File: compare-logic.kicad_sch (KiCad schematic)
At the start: 18 parts, among them U21001 4069, U21002 4019

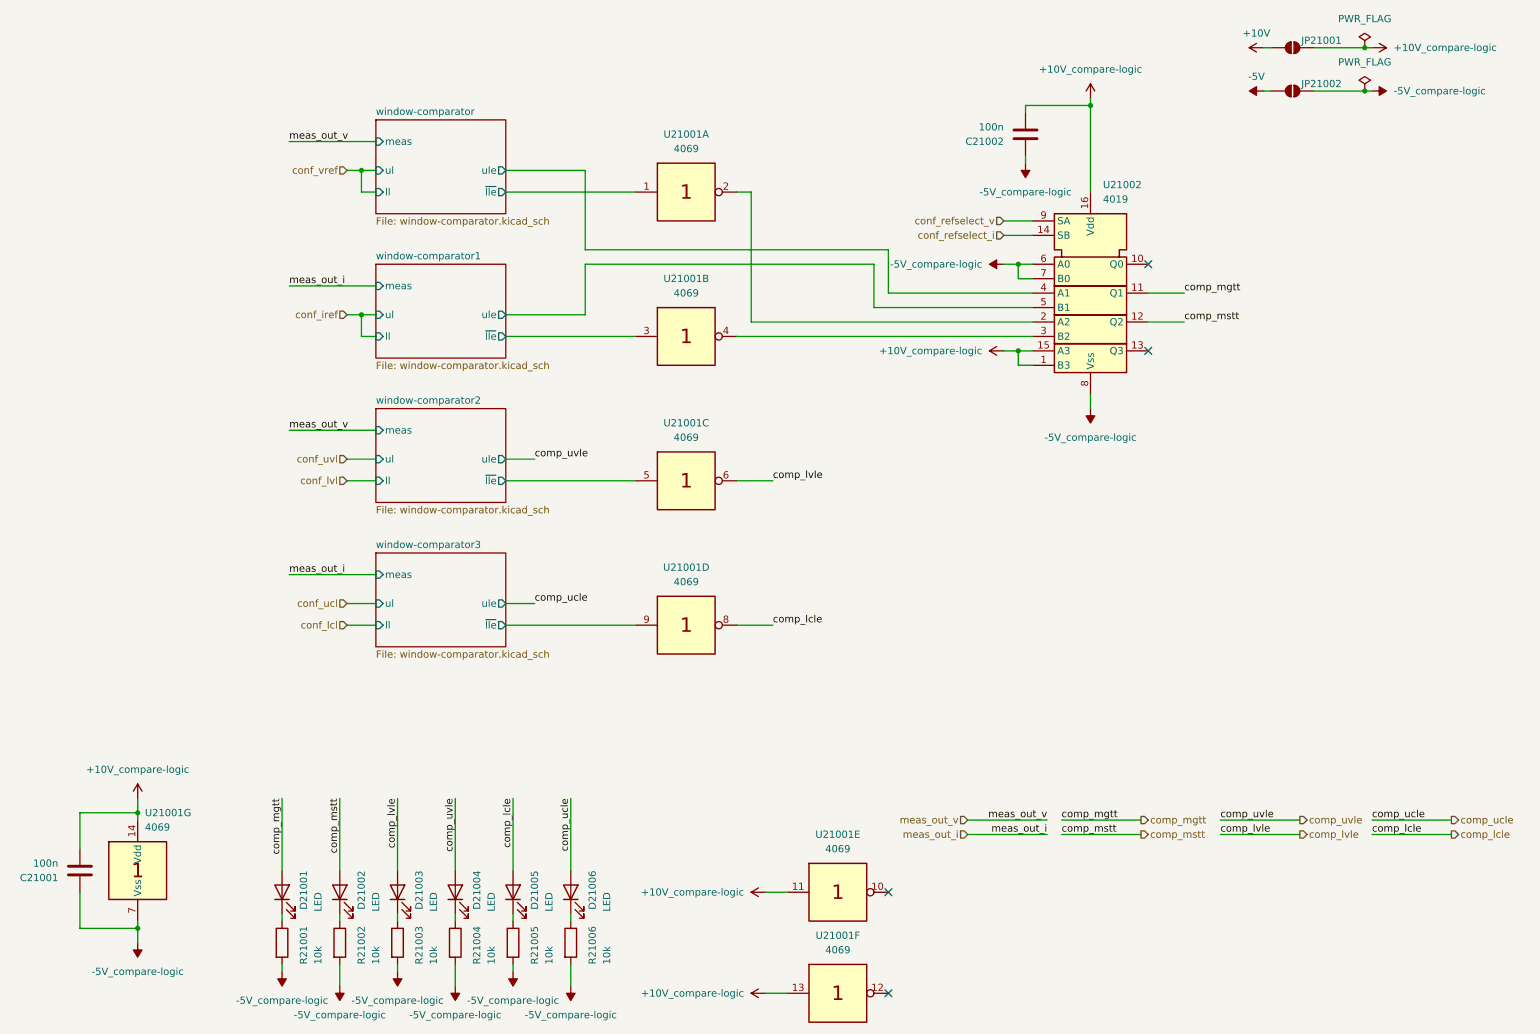
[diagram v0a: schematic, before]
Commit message: add pss 3dmodels and testpoints
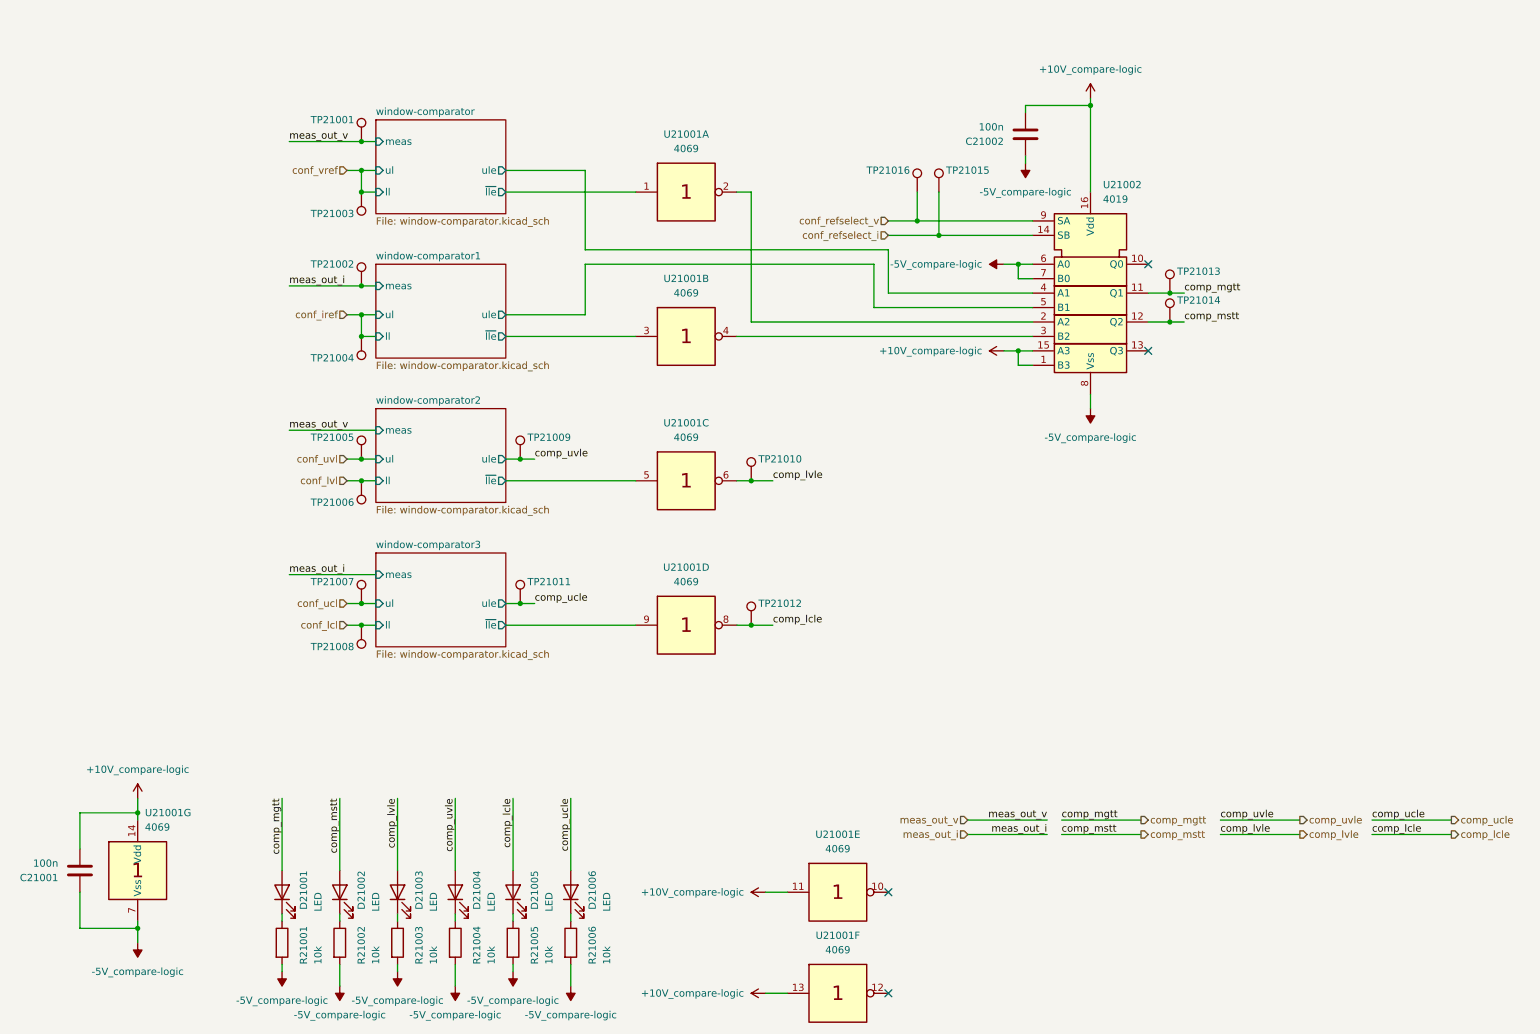
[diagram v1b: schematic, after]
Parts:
- removed JP21001, JP21002: SolderJumper_2_Open, symbol Jumper:SolderJumper_2_Open
- added TP21001, TP21002, TP21003, TP21004, TP21005, TP21006, TP21007, TP21008, TP21009, TP21010, TP21011, TP21012, TP21013, TP21014, TP21015, TP21016: ~, pss:TP_0805_2012Metric, symbol Connector:TestPoint
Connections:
- net comp_lcle: now also TP21012.1
- net comp_lvle: now also TP21010.1
- net comp_mgtt: now also TP21013.1
- net comp_mstt: now also TP21014.1
- net comp_ucle: now also TP21011.1
- net comp_uvle: now also TP21009.1
- net conf_iref: now also TP21004.1
- net conf_lcl: now also TP21008.1
- net conf_lvl: now also TP21006.1
- net conf_refselect_i: now also TP21015.1
- net conf_refselect_v: now also TP21016.1
- net conf_ucl: now also TP21007.1
- net conf_uvl: now also TP21005.1
- net conf_vref: now also TP21003.1
- net meas_out_i: now also TP21002.1
- net meas_out_v: now also TP21001.1

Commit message: edit pss symbol library: export all schematic symbols to library 'pss' and update symbol link
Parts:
- D21001, D21002, D21003, D21004, D21005, D21006: symbol Device:LED -> pss:LED
- TP21001, TP21002, TP21003, TP21004, TP21005, TP21006, TP21007, TP21008, TP21009, TP21010, TP21011, TP21012, TP21013, TP21014, TP21015, TP21016: symbol Connector:TestPoint -> pss:TestPoint
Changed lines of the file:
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@@
 	)
 	(symbol
-		(lib_id "Connector:TestPoint")
+		(lib_id "pss:TestPoint")
 		(at 222.25 67.31 0)
 		(unit 1)
@@
 	)
 	(symbol
-		(lib_id "Connector:TestPoint")
+		(lib_id "pss:TestPoint")
 		(at 181.61 49.53 0)
 		(unit 1)
@@
 	)
 	(symbol
-		(lib_id "Connector:TestPoint")
+		(lib_id "pss:TestPoint")
 		(at 80.01 125.73 180)
 		(unit 1)
@@
 	)
 	(symbol
-		(lib_id "Device:LED")
+		(lib_id "pss:LED")
 		(at 116.84 172.72 90)
 		(unit 1)
@@
 	)
 	(symbol
-		(lib_id "Connector:TestPoint")
+		(lib_id "pss:TestPoint")
 		(at 80.01 49.53 180)
 		(unit 1)
@@
 	)
 	(symbol
-		(lib_id "Connector:TestPoint")
+		(lib_id "pss:TestPoint")
 		(at 177.8 49.53 0)
 		(mirror y)
@@
 	)
 	(symbol
-		(lib_id "Connector:TestPoint")
+		(lib_id "pss:TestPoint")
 		(at 107.95 121.92 0)
 		(unit 1)
@@
 	)
 	(symbol
-		(lib_id "Connector:TestPoint")
+		(lib_id "pss:TestPoint")
 		(at 80.01 66.04 0)
 		(mirror y)
@@
 	)
 	(symbol
-		(lib_id "Connector:TestPoint")
+		(lib_id "pss:TestPoint")
 		(at 80.01 100.33 180)
 		(unit 1)
@@
 	)
 	(symbol
-		(lib_id "Device:LED")
+		(lib_id "pss:LED")
 		(at 96.52 172.72 90)
 		(unit 1)
@@
 	)
 	(symbol
-		(lib_id "Connector:TestPoint")
+		(lib_id "pss:TestPoint")
 		(at 107.95 96.52 0)
 		(unit 1)
@@
 	)
 	(symbol
-		(lib_id "Connector:TestPoint")
+		(lib_id "pss:TestPoint")
 		(at 80.01 121.92 0)
 		(mirror y)
@@
 	)
 	(symbol
-		(lib_id "Connector:TestPoint")
+		(lib_id "pss:TestPoint")
 		(at 80.01 74.93 180)
 		(unit 1)
@@
 	)
 	(symbol
-		(lib_id "Connector:TestPoint")
+		(lib_id "pss:TestPoint")
 		(at 80.01 96.52 0)
 		(mirror y)
@@
 	)
 	(symbol
-		(lib_id "Connector:TestPoint")
+		(lib_id "pss:TestPoint")
 		(at 222.25 72.39 0)
 		(unit 1)
@@
 	)
 	(symbol
-		(lib_id "Device:LED")
+		(lib_id "pss:LED")
 		(at 76.2 172.72 90)
 		(unit 1)
@@
 	)
 	(symbol
-		(lib_id "Connector:TestPoint")
+		(lib_id "pss:TestPoint")
 		(at 148.59 125.73 0)
 		(unit 1)
@@
 	)
 	(symbol
-		(lib_id "Device:LED")
+		(lib_id "pss:LED")
 		(at 106.68 172.72 90)
 		(unit 1)
@@
 	)
 	(symbol
-		(lib_id "Connector:TestPoint")
+		(lib_id "pss:TestPoint")
 		(at 80.01 40.64 0)
 		(mirror y)
@@
 	)
 	(symbol
-		(lib_id "Device:LED")
+		(lib_id "pss:LED")
 		(at 66.04 172.72 90)
 		(unit 1)
@@
 	)
 	(symbol
-		(lib_id "Connector:TestPoint")
+		(lib_id "pss:TestPoint")
 		(at 148.59 100.33 0)
 		(unit 1)
@@
 	)
 	(symbol
-		(lib_id "Device:LED")
+		(lib_id "pss:LED")
 		(at 86.36 172.72 90)
 		(unit 1)

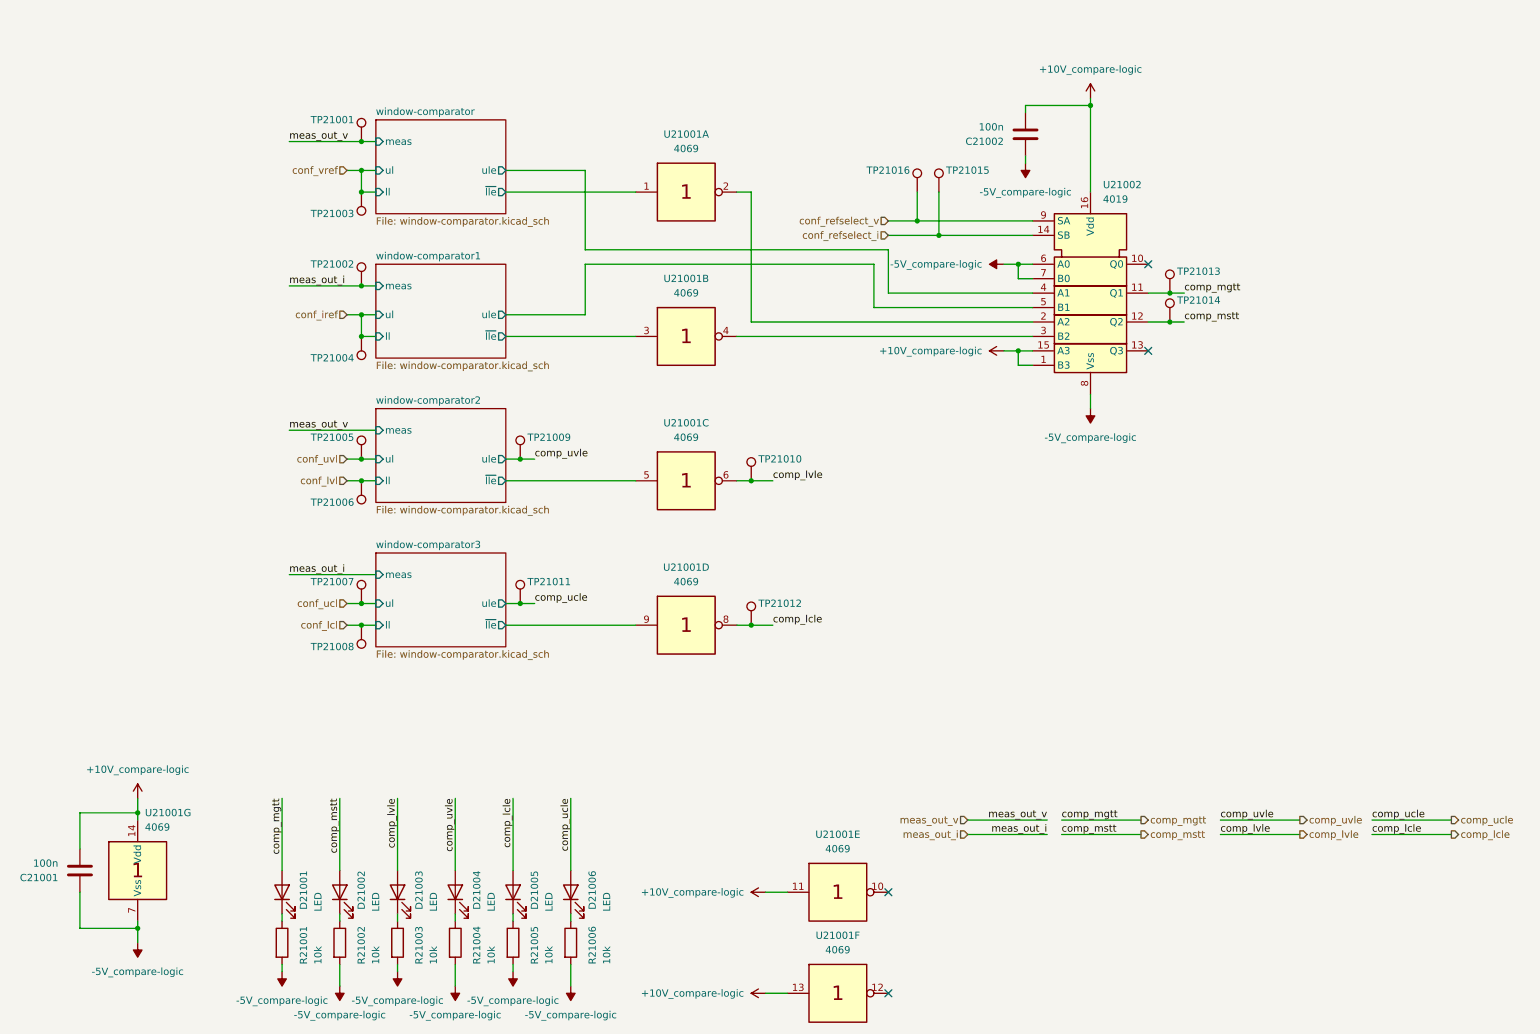
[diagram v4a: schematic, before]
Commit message: edit pss footprint library: export all footprints to library 'pss' and update footprint links
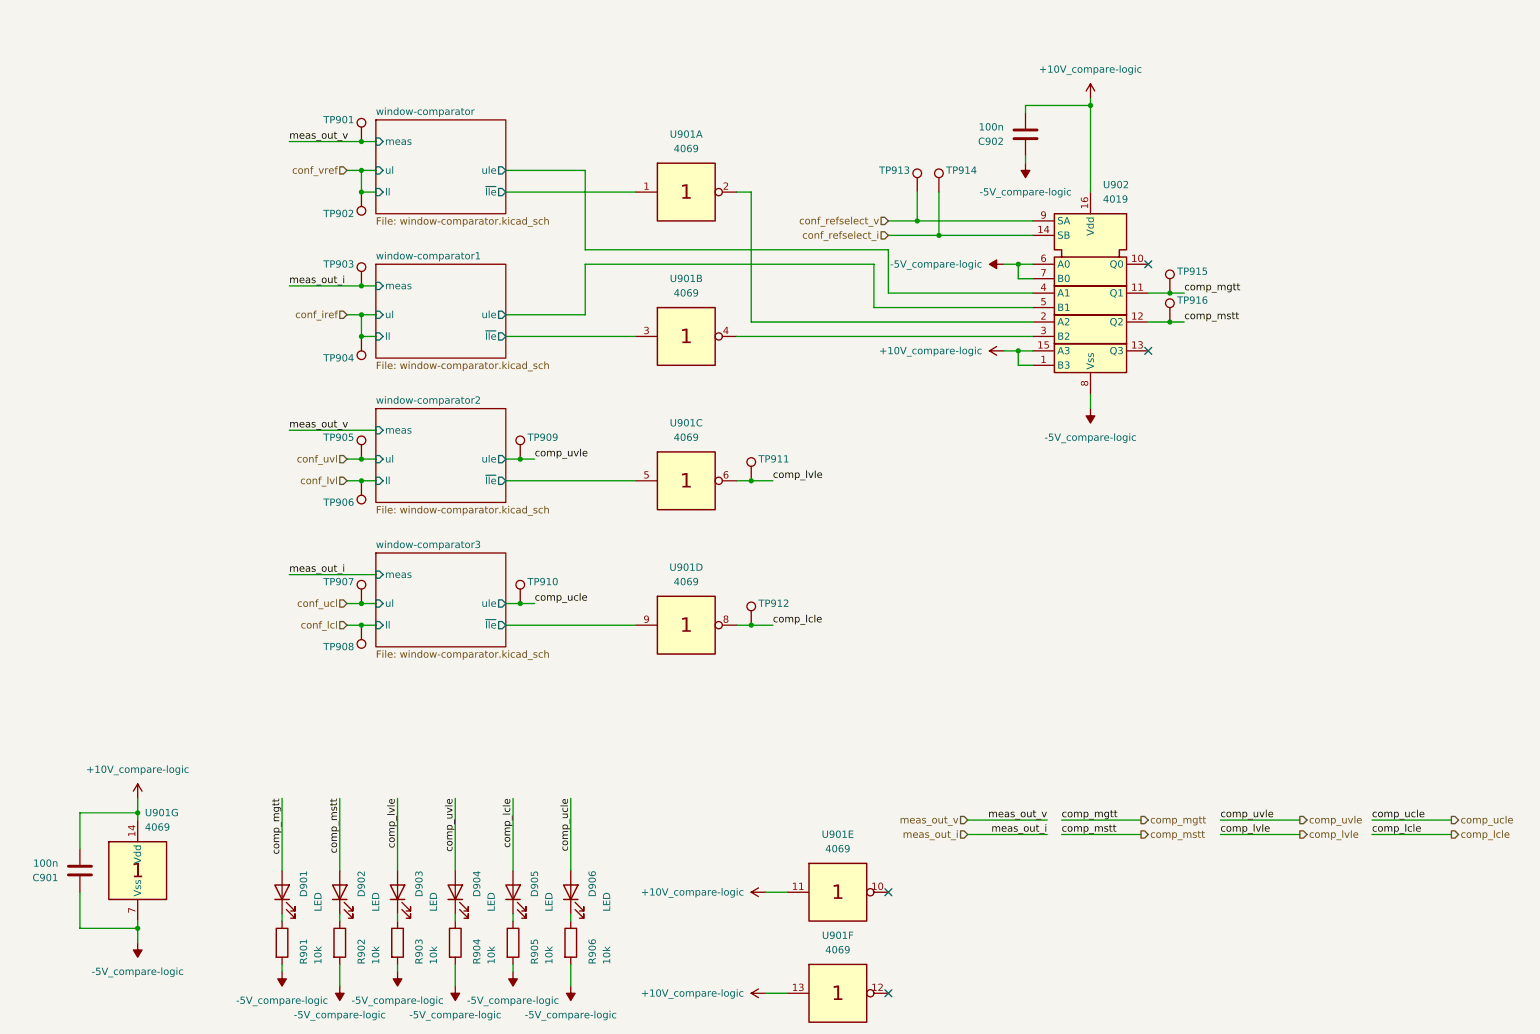
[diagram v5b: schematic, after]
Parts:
- C901: renamed from C21001; footprint Capacitor_SMD:C_0805_2012Metric_Pad1.18x1.45mm_HandSolder -> pss:C_0805_2012Metric_Pad1.18x1.45mm_HandSolder
- C902: renamed from C21002; footprint Capacitor_SMD:C_0805_2012Metric_Pad1.18x1.45mm_HandSolder -> pss:C_0805_2012Metric_Pad1.18x1.45mm_HandSolder
- D901: renamed from D21001; footprint LED_SMD:LED_0805_2012Metric_Pad1.15x1.40mm_HandSolder -> pss:LED_0805_2012Metric_Pad1.15x1.40mm_HandSolder
- D902: renamed from D21002; footprint LED_SMD:LED_0805_2012Metric_Pad1.15x1.40mm_HandSolder -> pss:LED_0805_2012Metric_Pad1.15x1.40mm_HandSolder
- D903: renamed from D21003; footprint LED_SMD:LED_0805_2012Metric_Pad1.15x1.40mm_HandSolder -> pss:LED_0805_2012Metric_Pad1.15x1.40mm_HandSolder
- D904: renamed from D21004; footprint LED_SMD:LED_0805_2012Metric_Pad1.15x1.40mm_HandSolder -> pss:LED_0805_2012Metric_Pad1.15x1.40mm_HandSolder
- D905: renamed from D21005; footprint LED_SMD:LED_0805_2012Metric_Pad1.15x1.40mm_HandSolder -> pss:LED_0805_2012Metric_Pad1.15x1.40mm_HandSolder
- D906: renamed from D21006; footprint LED_SMD:LED_0805_2012Metric_Pad1.15x1.40mm_HandSolder -> pss:LED_0805_2012Metric_Pad1.15x1.40mm_HandSolder
- R901: renamed from R21001; footprint Resistor_SMD:R_1210_3225Metric_Pad1.30x2.65mm_HandSolder -> pss:R_1210_3225Metric_Pad1.30x2.65mm_HandSolder
- R902: renamed from R21002; footprint Resistor_SMD:R_1210_3225Metric_Pad1.30x2.65mm_HandSolder -> pss:R_1210_3225Metric_Pad1.30x2.65mm_HandSolder
- R903: renamed from R21003; footprint Resistor_SMD:R_1210_3225Metric_Pad1.30x2.65mm_HandSolder -> pss:R_1210_3225Metric_Pad1.30x2.65mm_HandSolder
- R904: renamed from R21004; footprint Resistor_SMD:R_1210_3225Metric_Pad1.30x2.65mm_HandSolder -> pss:R_1210_3225Metric_Pad1.30x2.65mm_HandSolder
- R905: renamed from R21005; footprint Resistor_SMD:R_1210_3225Metric_Pad1.30x2.65mm_HandSolder -> pss:R_1210_3225Metric_Pad1.30x2.65mm_HandSolder
- R906: renamed from R21006; footprint Resistor_SMD:R_1210_3225Metric_Pad1.30x2.65mm_HandSolder -> pss:R_1210_3225Metric_Pad1.30x2.65mm_HandSolder
- U901: renamed from U21001; footprint Package_SO:SOIC-14_3.9x8.7mm_P1.27mm -> pss:SOIC-14_3.9x8.7mm_P1.27mm
- U902: renamed from U21002; footprint Package_SO:SOIC-16_3.9x9.9mm_P1.27mm -> pss:SOIC-16_3.9x9.9mm_P1.27mm
- renumbered TP21001 to TP901, TP21003 to TP902, TP21002 to TP903, TP21004 to TP904, TP21005 to TP905, TP21006 to TP906, TP21007 to TP907, TP21008 to TP908, TP21009 to TP909, TP21011 to TP910, TP21010 to TP911, TP21012 to TP912, TP21016 to TP913, TP21015 to TP914, TP21013 to TP915, TP21014 to TP916
